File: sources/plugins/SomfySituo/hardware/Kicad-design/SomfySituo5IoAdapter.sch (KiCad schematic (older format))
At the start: 30 parts, among them J1 USB_OTG, J10 Conn_01x01, J11 Conn_01x01, J12 Conn_01x01, J13 Conn_01x01, J15 ICSP, J2 Conn_01x01, J3 Conn_01x01, J4 Conn_01x01, J5 Conn_01x01, J6 Conn_01x01, J7 Conn_01x01, J8 Conn_01x01, J9 Conn_01x01, U1 FT230X, U2 PIC16F688

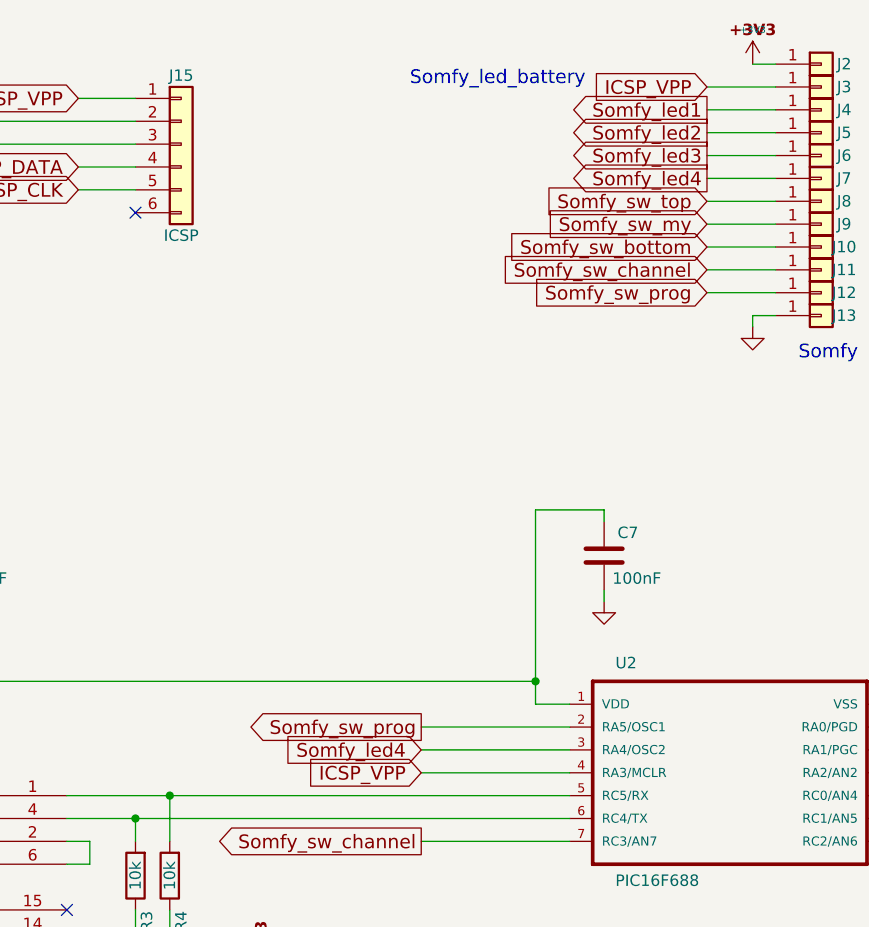
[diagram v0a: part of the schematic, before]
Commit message: Fix output leds and serigraphy
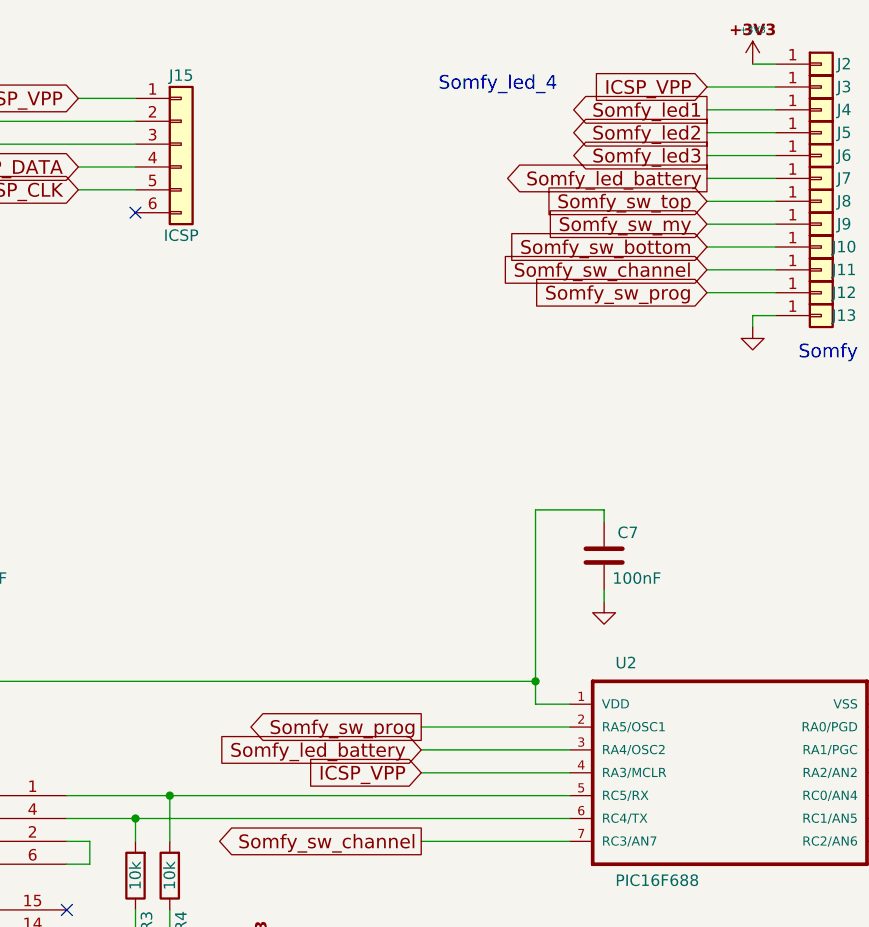
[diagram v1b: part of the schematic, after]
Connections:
- net Somfy_led4 renamed Somfy_led_battery
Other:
- note added: "Somfy_led_4"
- note removed: "Somfy_led_battery"
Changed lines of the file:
@@
 LIBS:contrib
 LIBS:valves
-LIBS:PIC16F688
-LIBS:ESD_Protection
-LIBS:serial
 LIBS:SomfySituo5IoAdapter-cache
 EELAYER 25 0
@@
 Somfy_led3
 Text GLabel 7250 4450 0    60   Input ~ 0
-Somfy_led4
+Somfy_led_battery
 $Comp
 L GND #PWR04
@@
 Somfy_led3
 Text GLabel 8500 1950 0    60   Output ~ 0
-Somfy_led4
+Somfy_led_battery
 Text GLabel 8500 2050 0    60   Input ~ 0
 Somfy_sw_top
@@
 	1    0    0    -1
 $EndComp
-Text Notes 7200 1550 0    60   ~ 0
-Somfy_led_battery
 Text Label 1350 4150 0    60   ~ 0
 VCC_IN
@@
 $EndComp
 Connection ~ 4300 1600
+Text Notes 7325 1575 0    60   ~ 0
+Somfy_led_4
 $EndSCHEMATC
